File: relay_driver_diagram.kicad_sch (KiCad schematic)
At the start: 3 parts, among them K1 5v Relay NO, U1 Raspberry Pi4b

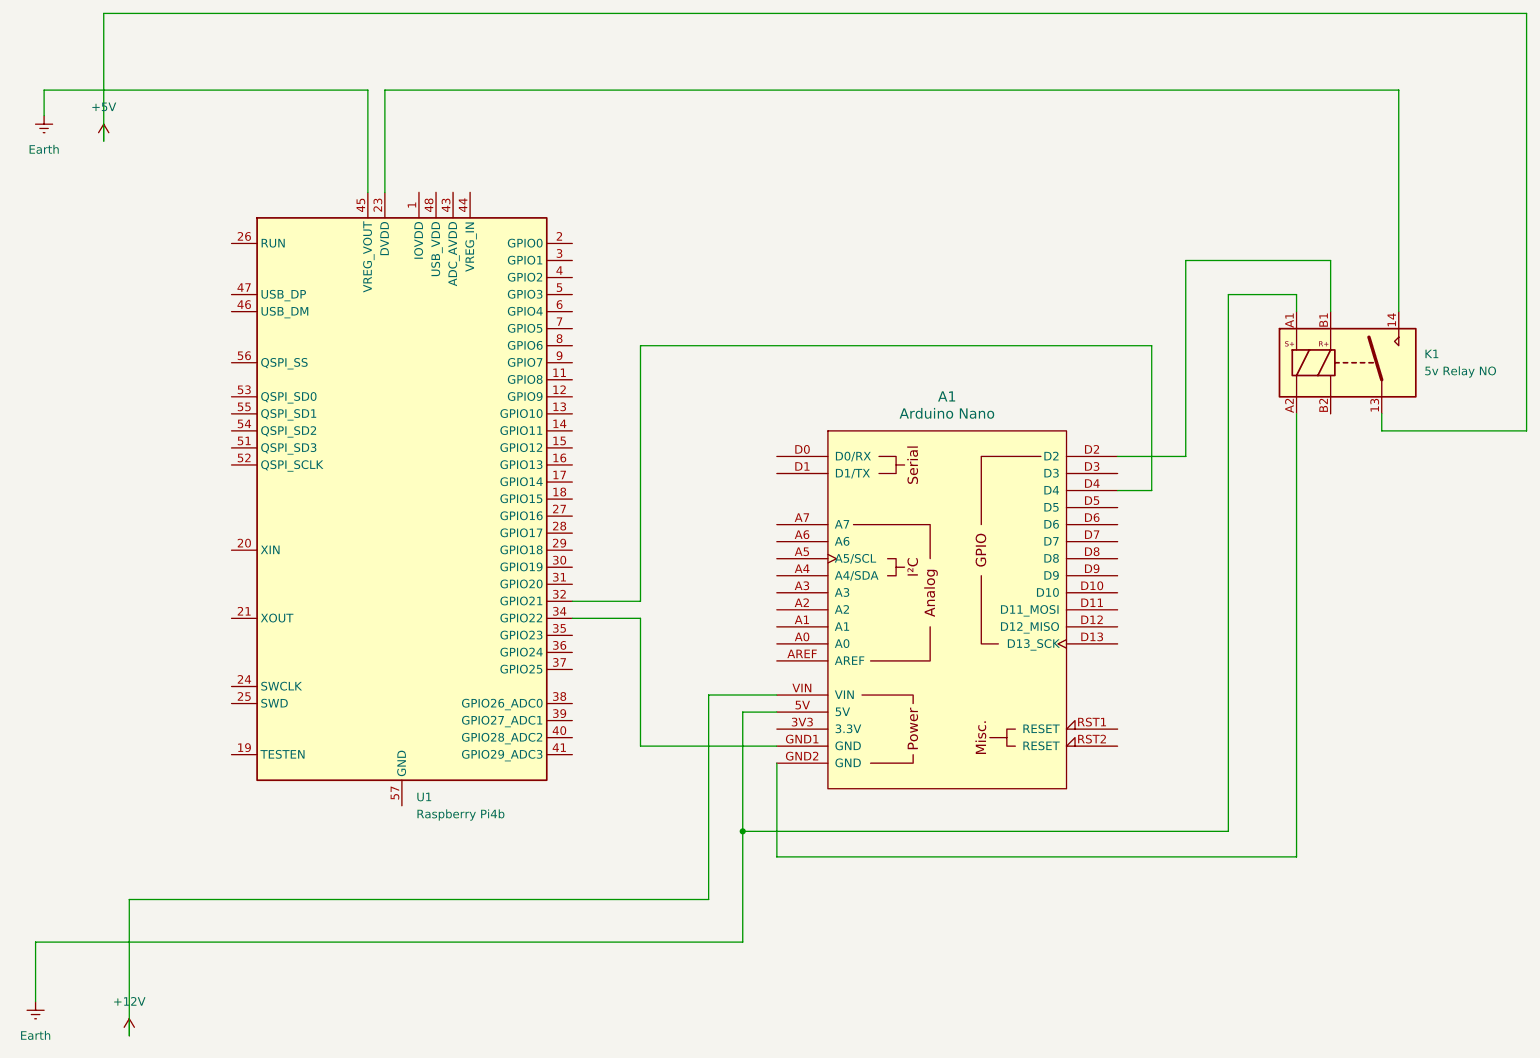
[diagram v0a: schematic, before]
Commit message: correct a couple of small errors in the diagram
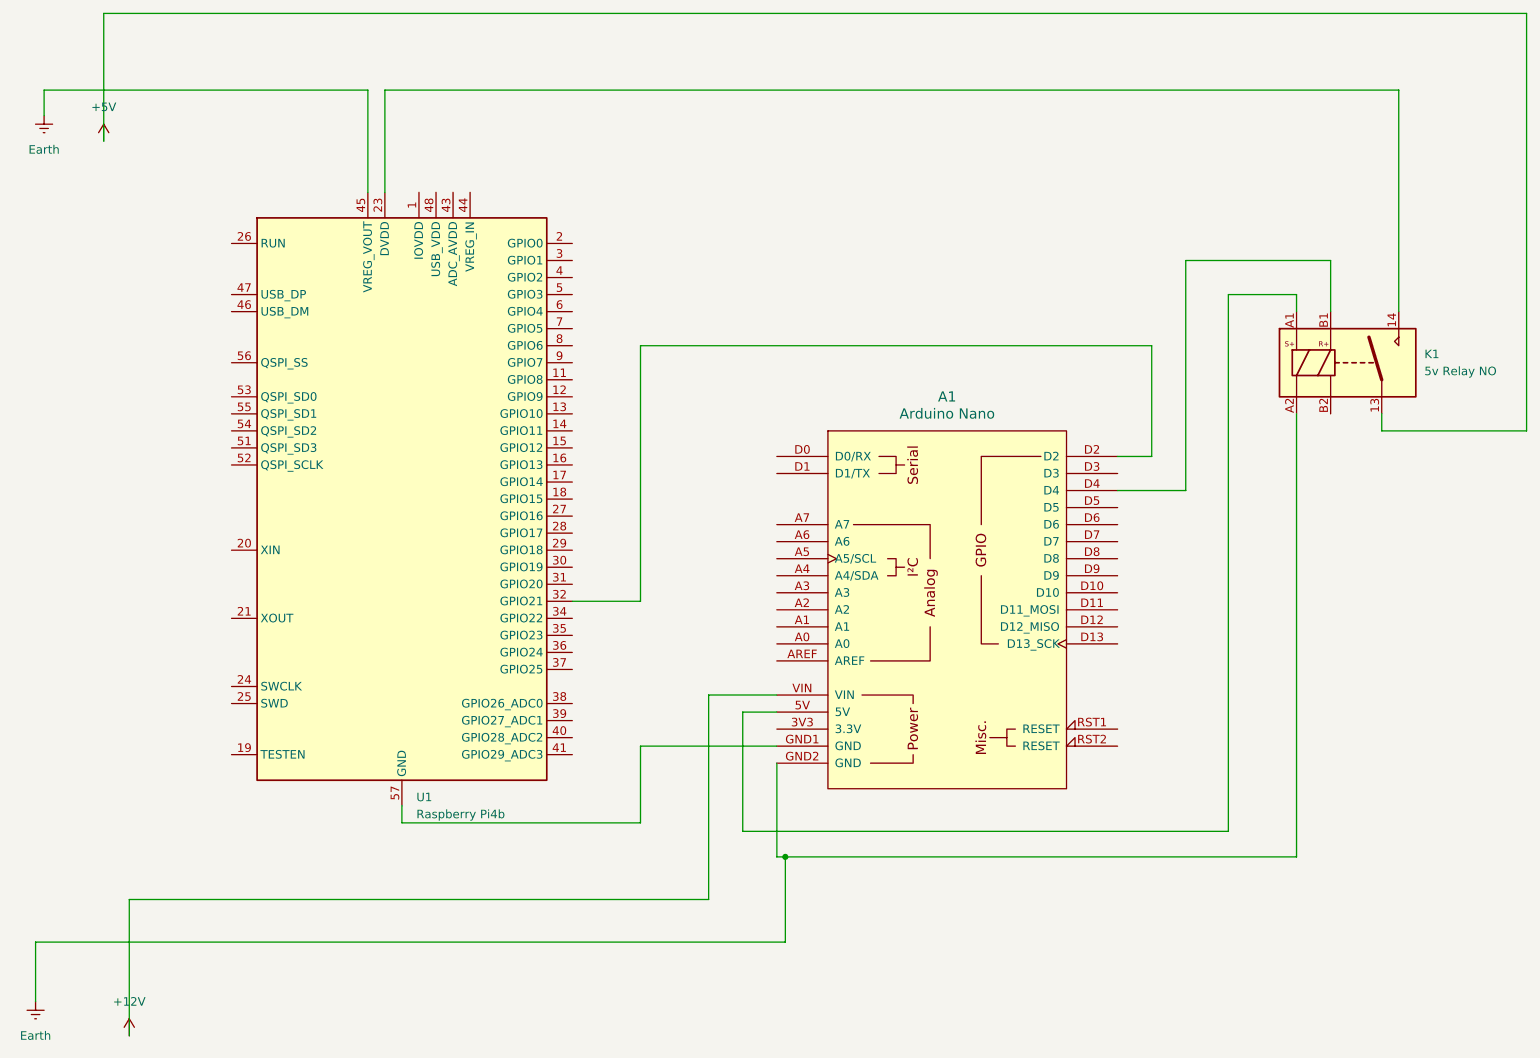
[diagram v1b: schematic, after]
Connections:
- net Earth: now also A1.GND2 (GND), K1.A2; no longer A1.5V, K1.A1
- net at U1.32 (GPIO21): now also A1.D2; no longer A1.D4
- net at U1.34 (GPIO22): no longer A1.GND1 (GND)
- net at U1.57 (GND): now also A1.GND1 (GND)
- net at K1.B1: now also A1.D4; no longer A1.D2
- new net: A1.5V, K1.A1
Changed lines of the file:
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@@
 	)
 	(junction
-		(at 129.54 148.59)
+		(at 135.89 152.4)
 		(diameter 0)
 		(color 0 0 0 0)
@@
 	(wire
 		(pts
-			(xy 190.5 97.79) (xy 185.42 97.79)
-		)
-		(stroke
-			(width 0)
-			(type default)
-		)
-	)
-	(wire
-		(pts
-			(xy 190.5 76.2) (xy 190.5 97.79)
+			(xy 195.58 97.79) (xy 185.42 97.79)
+		)
+		(stroke
+			(width 0)
+			(type default)
+		)
+	)
+	(wire
+		(pts
+			(xy 78.74 147.32) (xy 78.74 144.78)
 		)
 		(stroke
@@
 	(wire
 		(pts
-			(xy 129.54 165.1) (xy 129.54 148.59)
-		)
-		(stroke
-			(width 0)
-			(type default)
-		)
-	)
-	(wire
-		(pts
 			(xy 227.33 71.12) (xy 227.33 38.1)
 		)
@@
 	(wire
 		(pts
-			(xy 24.13 165.1) (xy 129.54 165.1)
-		)
-		(stroke
-			(width 0)
-			(type default)
-		)
-	)
-	(wire
-		(pts
-			(xy 195.58 92.71) (xy 195.58 63.5)
-		)
-		(stroke
-			(width 0)
-			(type default)
-		)
-	)
-	(wire
-		(pts
 			(xy 201.93 148.59) (xy 201.93 68.58)
 		)
@@
 	(wire
 		(pts
-			(xy 114.3 116.84) (xy 114.3 135.89)
-		)
-		(stroke
-			(width 0)
-			(type default)
-		)
-	)
-	(wire
-		(pts
 			(xy 73.66 53.34) (xy 73.66 38.1)
 		)
@@
 	(wire
 		(pts
-			(xy 185.42 92.71) (xy 195.58 92.71)
-		)
-		(stroke
-			(width 0)
-			(type default)
-		)
-	)
-	(wire
-		(pts
 			(xy 34.29 26.67) (xy 246.38 26.67)
 		)
@@
 	(wire
 		(pts
+			(xy 195.58 63.5) (xy 195.58 97.79)
+		)
+		(stroke
+			(width 0)
+			(type default)
+		)
+	)
+	(wire
+		(pts
 			(xy 124.46 158.75) (xy 124.46 128.27)
 		)
@@
 	(wire
 		(pts
-			(xy 212.09 152.4) (xy 134.62 152.4)
+			(xy 185.42 92.71) (xy 190.5 92.71)
+		)
+		(stroke
+			(width 0)
+			(type default)
+		)
+	)
+	(wire
+		(pts
+			(xy 212.09 152.4) (xy 135.89 152.4)
+		)
+		(stroke
+			(width 0)
+			(type default)
+		)
+	)
+	(wire
+		(pts
+			(xy 135.89 152.4) (xy 134.62 152.4)
 		)
 		(stroke
@@
 	(wire
 		(pts
-			(xy 104.14 116.84) (xy 114.3 116.84)
+			(xy 190.5 92.71) (xy 190.5 76.2)
 		)
 		(stroke
@@
 	(wire
 		(pts
+			(xy 114.3 147.32) (xy 78.74 147.32)
+		)
+		(stroke
+			(width 0)
+			(type default)
+		)
+	)
+	(wire
+		(pts
 			(xy 129.54 130.81) (xy 129.54 148.59)
 		)
@@
 	(wire
 		(pts
+			(xy 114.3 135.89) (xy 114.3 147.32)
+		)
+		(stroke
+			(width 0)
+			(type default)
+		)
+	)
+	(wire
+		(pts
 			(xy 134.62 130.81) (xy 129.54 130.81)
 		)
@@
 	(wire
 		(pts
+			(xy 24.13 165.1) (xy 135.89 165.1)
+		)
+		(stroke
+			(width 0)
+			(type default)
+		)
+	)
+	(wire
+		(pts
 			(xy 212.09 86.36) (xy 212.09 152.4)
 		)
@@
 		)
 		(stroke
+			(width 0)
+			(type default)
+		)
+	)
+	(wire
+		(pts
+			(xy 135.89 165.1) (xy 135.89 152.4)
+		)
+		(stroke
